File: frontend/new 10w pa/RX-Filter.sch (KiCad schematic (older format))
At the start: 96 parts, among them Q4 FDV301, U3 74LS145

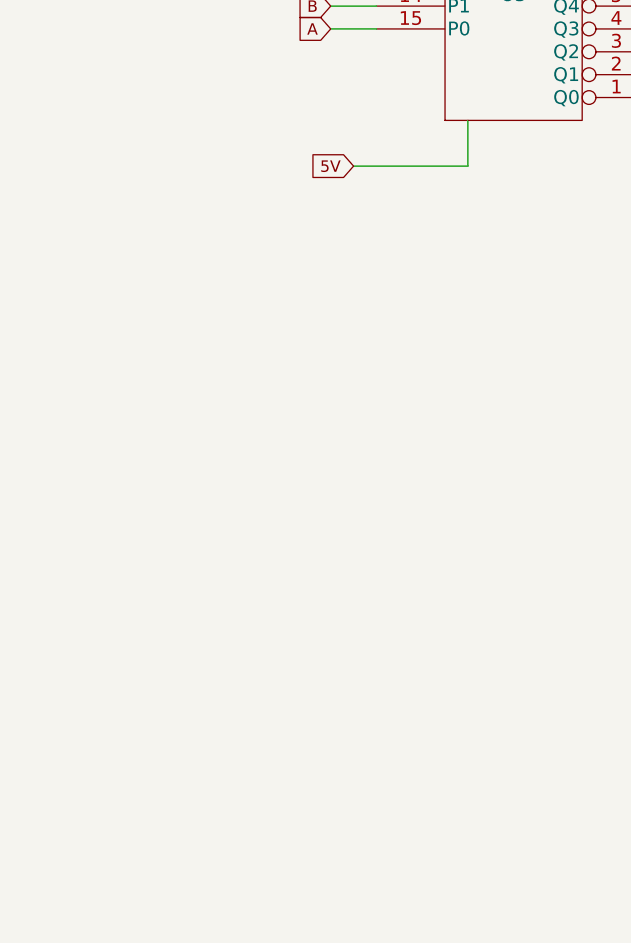
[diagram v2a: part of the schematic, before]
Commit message: Added opto and change of PTT
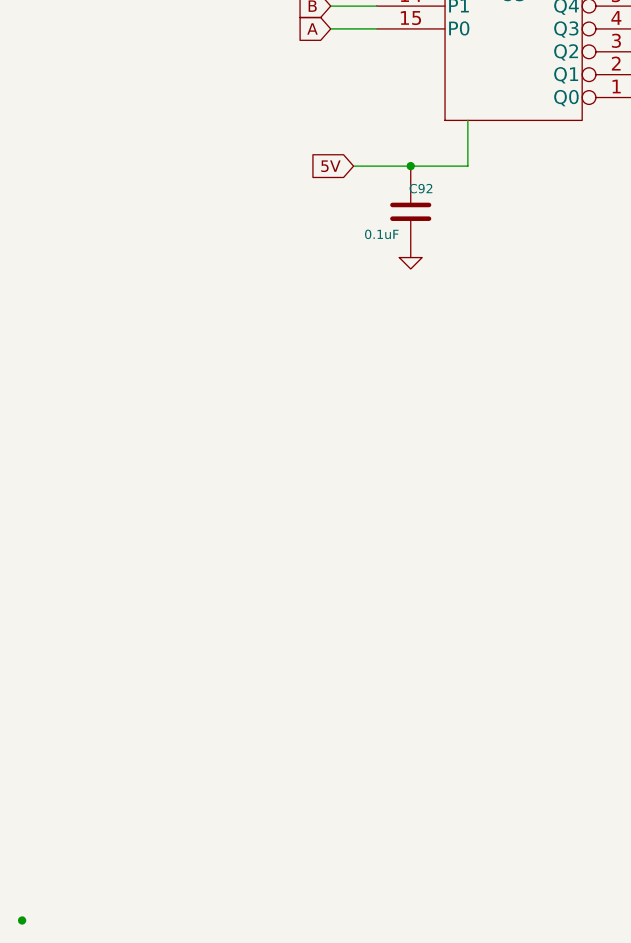
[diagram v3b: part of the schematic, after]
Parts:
- added C92: 0.1uF, HERMESLITE:C_0805, symbol C
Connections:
- net GND: now also C92.1
- net VCC: now also C92.2
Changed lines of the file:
@@
 $EndComp
 $Comp
-L GND #PWR045
+L GND #PWR052
 U 1 1 54A26D4B
 P 7800 2700
-F 0 "#PWR045" H 7800 2700 30  0001 C CNN
+F 0 "#PWR052" H 7800 2700 30  0001 C CNN
 F 1 "GND" H 7800 2630 30  0001 C CNN
 F 2 "" H 7800 2700 50  0000 C CNN
@@
 $EndComp
 $Comp
-L GND #PWR046
+L GND #PWR053
 U 1 1 54A26D51
 P 6550 2700
-F 0 "#PWR046" H 6550 2700 30  0001 C CNN
+F 0 "#PWR053" H 6550 2700 30  0001 C CNN
 F 1 "GND" H 6550 2630 30  0001 C CNN
 F 2 "" H 6550 2700 50  0000 C CNN
@@
 $EndComp
 $Comp
-L GND #PWR047
+L GND #PWR054
 U 1 1 54A26D57
 P 6300 2900
-F 0 "#PWR047" H 6300 2900 30  0001 C CNN
+F 0 "#PWR054" H 6300 2900 30  0001 C CNN
 F 1 "GND" H 6300 2830 30  0001 C CNN
 F 2 "" H 6300 2900 50  0000 C CNN
@@
 $EndComp
 $Comp
-L GND #PWR048
+L GND #PWR055
 U 1 1 54A26D5D
 P 5300 2700
-F 0 "#PWR048" H 5300 2700 30  0001 C CNN
+F 0 "#PWR055" H 5300 2700 30  0001 C CNN
 F 1 "GND" H 5300 2630 30  0001 C CNN
 F 2 "" H 5300 2700 50  0000 C CNN
@@
 $EndComp
 $Comp
-L GND #PWR049
+L GND #PWR056
 U 1 1 54A26D72
 P 4650 3000
-F 0 "#PWR049" H 4650 3000 30  0001 C CNN
+F 0 "#PWR056" H 4650 3000 30  0001 C CNN
 F 1 "GND" H 4650 2930 30  0001 C CNN
 F 2 "" H 4650 3000 50  0000 C CNN
@@
 $EndComp
 $Comp
-L GND #PWR050
+L GND #PWR057
 U 1 1 54A26D78
 P 7950 3000
-F 0 "#PWR050" H 7950 3000 30  0001 C CNN
+F 0 "#PWR057" H 7950 3000 30  0001 C CNN
 F 1 "GND" H 7950 2930 30  0001 C CNN
 F 2 "" H 7950 3000 50  0000 C CNN
@@
 $EndComp
 $Comp
-L GND #PWR051
+L GND #PWR058
 U 1 1 54A28AFC
 P 7800 4700
-F 0 "#PWR051" H 7800 4700 30  0001 C CNN
+F 0 "#PWR058" H 7800 4700 30  0001 C CNN
 F 1 "GND" H 7800 4630 30  0001 C CNN
 F 2 "" H 7800 4700 50  0000 C CNN
@@
 $EndComp
 $Comp
-L GND #PWR052
+L GND #PWR059
 U 1 1 54A28B02
 P 6550 4700
-F 0 "#PWR052" H 6550 4700 30  0001 C CNN
+F 0 "#PWR059" H 6550 4700 30  0001 C CNN
 F 1 "GND" H 6550 4630 30  0001 C CNN
 F 2 "" H 6550 4700 50  0000 C CNN
@@
 $EndComp
 $Comp
-L GND #PWR053
+L GND #PWR060
 U 1 1 54A28B08
 P 6300 4900
-F 0 "#PWR053" H 6300 4900 30  0001 C CNN
+F 0 "#PWR060" H 6300 4900 30  0001 C CNN
 F 1 "GND" H 6300 4830 30  0001 C CNN
 F 2 "" H 6300 4900 50  0000 C CNN
@@
 $EndComp
 $Comp
-L GND #PWR054
+L GND #PWR061
 U 1 1 54A28B0E
 P 5300 4700
-F 0 "#PWR054" H 5300 4700 30  0001 C CNN
+F 0 "#PWR061" H 5300 4700 30  0001 C CNN
 F 1 "GND" H 5300 4630 30  0001 C CNN
 F 2 "" H 5300 4700 50  0000 C CNN
@@
 $EndComp
 $Comp
-L GND #PWR055
+L GND #PWR062
 U 1 1 54A28B21
 P 4650 5000
-F 0 "#PWR055" H 4650 5000 30  0001 C CNN
+F 0 "#PWR062" H 4650 5000 30  0001 C CNN
 F 1 "GND" H 4650 4930 30  0001 C CNN
 F 2 "" H 4650 5000 50  0000 C CNN
@@
 $EndComp
 $Comp
-L GND #PWR056
+L GND #PWR063
 U 1 1 54A28B27
 P 7950 5000
-F 0 "#PWR056" H 7950 5000 30  0001 C CNN
+F 0 "#PWR063" H 7950 5000 30  0001 C CNN
 F 1 "GND" H 7950 4930 30  0001 C CNN
 F 2 "" H 7950 5000 50  0000 C CNN
@@
 $EndComp
 $Comp
-L GND #PWR057
+L GND #PWR064
 U 1 1 54A2A84A
 P 7800 3700
-F 0 "#PWR057" H 7800 3700 30  0001 C CNN
+F 0 "#PWR064" H 7800 3700 30  0001 C CNN
 F 1 "GND" H 7800 3630 30  0001 C CNN
 F 2 "" H 7800 3700 50  0000 C CNN
@@
 $EndComp
 $Comp
-L GND #PWR058
+L GND #PWR065
 U 1 1 54A2A850
 P 6550 3700
-F 0 "#PWR058" H 6550 3700 30  0001 C CNN
+F 0 "#PWR065" H 6550 3700 30  0001 C CNN
 F 1 "GND" H 6550 3630 30  0001 C CNN
 F 2 "" H 6550 3700 50  0000 C CNN
@@
 $EndComp
 $Comp
-L GND #PWR059
+L GND #PWR066
 U 1 1 54A2A856
 P 6300 3900
-F 0 "#PWR059" H 6300 3900 30  0001 C CNN
+F 0 "#PWR066" H 6300 3900 30  0001 C CNN
 F 1 "GND" H 6300 3830 30  0001 C CNN
 F 2 "" H 6300 3900 50  0000 C CNN
@@
 $EndComp
 $Comp
-L GND #PWR060
+L GND #PWR067
 U 1 1 54A2A85C
 P 5300 3700
-F 0 "#PWR060" H 5300 3700 30  0001 C CNN
+F 0 "#PWR067" H 5300 3700 30  0001 C CNN
 F 1 "GND" H 5300 3630 30  0001 C CNN
 F 2 "" H 5300 3700 50  0000 C CNN
@@
 $EndComp
 $Comp
-L GND #PWR061
+L GND #PWR068
 U 1 1 54A2A86F
 P 4650 4000
-F 0 "#PWR061" H 4650 4000 30  0001 C CNN
+F 0 "#PWR068" H 4650 4000 30  0001 C CNN
 F 1 "GND" H 4650 3930 30  0001 C CNN
 F 2 "" H 4650 4000 50  0000 C CNN
@@
 $EndComp
 $Comp
-L GND #PWR062
+L GND #PWR069
 U 1 1 54A2A875
 P 7950 4000
-F 0 "#PWR062" H 7950 4000 30  0001 C CNN
+F 0 "#PWR069" H 7950 4000 30  0001 C CNN
 F 1 "GND" H 7950 3930 30  0001 C CNN
 F 2 "" H 7950 4000 50  0000 C CNN
@@
 $EndComp
 $Comp
-L GND #PWR063
+L GND #PWR070
 U 1 1 54A2AFAC
 P 7800 5700
-F 0 "#PWR063" H 7800 5700 30  0001 C CNN
+F 0 "#PWR070" H 7800 5700 30  0001 C CNN
 F 1 "GND" H 7800 5630 30  0001 C CNN
 F 2 "" H 7800 5700 50  0000 C CNN
@@
 $EndComp
 $Comp
-L GND #PWR064
+L GND #PWR071
 U 1 1 54A2AFB2
 P 6550 5700
-F 0 "#PWR064" H 6550 5700 30  0001 C CNN
+F 0 "#PWR071" H 6550 5700 30  0001 C CNN
 F 1 "GND" H 6550 5630 30  0001 C CNN
 F 2 "" H 6550 5700 50  0000 C CNN
@@
 $EndComp
 $Comp
-L GND #PWR065
+L GND #PWR072
 U 1 1 54A2AFB8
 P 6300 5900
-F 0 "#PWR065" H 6300 5900 30  0001 C CNN
+F 0 "#PWR072" H 6300 5900 30  0001 C CNN
 F 1 "GND" H 6300 5830 30  0001 C CNN
 F 2 "" H 6300 5900 50  0000 C CNN
@@
 $EndComp
 $Comp
-L GND #PWR066
+L GND #PWR073
 U 1 1 54A2AFBE
 P 5200 5700
-F 0 "#PWR066" H 5200 5700 30  0001 C CNN
+F 0 "#PWR073" H 5200 5700 30  0001 C CNN
 F 1 "GND" H 5200 5630 30  0001 C CNN
 F 2 "" H 5200 5700 50  0000 C CNN
@@
 $EndComp
 $Comp
-L GND #PWR067
+L GND #PWR074
 U 1 1 54A2AFD1
 P 4600 6000
-F 0 "#PWR067" H 4600 6000 30  0001 C CNN
+F 0 "#PWR074" H 4600 6000 30  0001 C CNN
 F 1 "GND" H 4600 5930 30  0001 C CNN
 F 2 "" H 4600 6000 50  0000 C CNN
@@
 $EndComp
 $Comp
-L GND #PWR068
+L GND #PWR075
 U 1 1 54A2AFD7
 P 8050 6000
-F 0 "#PWR068" H 8050 6000 30  0001 C CNN
+F 0 "#PWR075" H 8050 6000 30  0001 C CNN
 F 1 "GND" H 8050 5930 30  0001 C CNN
 F 2 "" H 8050 6000 50  0000 C CNN
@@
 $EndComp
 $Comp
-L GND #PWR069
+L GND #PWR076
 U 1 1 54A2CBBC
 P 6550 6700
-F 0 "#PWR069" H 6550 6700 30  0001 C CNN
+F 0 "#PWR076" H 6550 6700 30  0001 C CNN
 F 1 "GND" H 6550 6630 30  0001 C CNN
 F 2 "" H 6550 6700 50  0000 C CNN
@@
 $EndComp
 $Comp
-L GND #PWR070
+L GND #PWR077
 U 1 1 54A2CBCE
 P 5300 6700
-F 0 "#PWR070" H 5300 6700 30  0001 C CNN
+F 0 "#PWR077" H 5300 6700 30  0001 C CNN
 F 1 "GND" H 5300 6630 30  0001 C CNN
 F 2 "" H 5300 6700 50  0000 C CNN
@@
 $EndComp
 $Comp
-L GND #PWR071
+L GND #PWR078
 U 1 1 54A2CBE1
 P 4650 7000
-F 0 "#PWR071" H 4650 7000 30  0001 C CNN
+F 0 "#PWR078" H 4650 7000 30  0001 C CNN
 F 1 "GND" H 4650 6930 30  0001 C CNN
 F 2 "" H 4650 7000 50  0000 C CNN
@@
 $EndComp
 $Comp
-L GND #PWR072
+L GND #PWR079
 U 1 1 54A2CBE7
 P 6800 7000
-F 0 "#PWR072" H 6800 7000 30  0001 C CNN
+F 0 "#PWR079" H 6800 7000 30  0001 C CNN
 F 1 "GND" H 6800 6930 30  0001 C CNN
 F 2 "" H 6800 7000 50  0000 C CNN
@@
 Filter Settings for PowerSDR Hermes Ctrl\n(set for RX and TX J16 Pins)\n        1  2  3  4 \nBypass 0  1  0  1 (or higher) \n160M   0  0  0  0\n80M    1  0  0  0\n60M    0  1  0  0\n40M    1  1  0  0\n30M    0  0  1  0\n20M    1  0  1  0\n17M    0  1  1  0\n15M    1  1  1  0\n12M    0  0  0  1\n10M    1  0  0  1
 $Comp
-L GND #PWR073
+L GND #PWR080
 U 1 1 54C1EBE4
 P 1150 3100
-F 0 "#PWR073" H 1150 3100 30  0001 C CNN
+F 0 "#PWR080" H 1150 3100 30  0001 C CNN
 F 1 "GND" H 1150 3030 30  0001 C CNN
 F 2 "" H 1150 3100 50  0000 C CNN
@@
 $EndComp
 $Comp
-L GND #PWR074
+L GND #PWR081
 U 1 1 54C3258A
 P 4900 2000
-F 0 "#PWR074" H 4900 2000 30  0001 C CNN
+F 0 "#PWR081" H 4900 2000 30  0001 C CNN
 F 1 "GND" H 4900 1930 30  0001 C CNN
 F 2 "" H 4900 2000 50  0000 C CNN
@@
 $EndComp
 $Comp
-L GND #PWR075
+L GND #PWR082
 U 1 1 54C32686
 P 7900 2000
-F 0 "#PWR075" H 7900 2000 30  0001 C CNN
+F 0 "#PWR082" H 7900 2000 30  0001 C CNN
 F 1 "GND" H 7900 1930 30  0001 C CNN
 F 2 "" H 7900 2000 50  0000 C CNN
@@
 	3200 1900 3100 1900
 $Comp
-L GND #PWR076
+L GND #PWR083
 U 1 1 54C40367
 P 3100 2400
-F 0 "#PWR076" H 3100 2400 30  0001 C CNN
+F 0 "#PWR083" H 3100 2400 30  0001 C CNN
 F 1 "GND" H 3100 2330 30  0001 C CNN
 F 2 "" H 3100 2400 50  0000 C CNN
@@
 	6300 6300 6300 6500
 Connection ~ 6350 6300
+$Comp
+L C C92
+U 1 1 54D8F694
+P 1150 4600
+F 0 "C92" H 1050 4500 40  0000 L CNN
+F 1 "0.1uF" H 1200 4700 40  0000 L CNN
+F 2 "HERMESLITE:C_0805" H 1188 4450 30  0001 C CNN
+F 3 "" H 1150 4600 60  0000 C CNN
+	1    1150 4600
+	-1   0    0    1
+$EndComp
+$Comp
+L GND #PWR084
+U 1 1 54D8FD7B
+P 1150 4800
+F 0 "#PWR084" H 1150 4800 30  0001 C CNN
+F 1 "GND" H 1150 4730 30  0001 C CNN
+F 2 "" H 1150 4800 50  0000 C CNN
+F 3 "" H 1150 4800 50  0000 C CNN
+	1    1150 4800
+	1    0    0    -1
+$EndComp
+Connection ~ 1150 4400
+Connection ~ -550 7700
 $EndSCHEMATC

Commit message: modify mounting holes
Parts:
- Q4: footprint SMD_Packages:SOT-23-GDS -> HERMESLITE:SOT-23-GDS
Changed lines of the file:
@@
 F 0 "Q4" H 3010 2270 60  0000 R CNN
 F 1 "FDV301" H 2850 2250 60  0000 R CNN
-F 2 "SMD_Packages:SOT-23-GDS" H 3000 2100 60  0001 C CNN
+F 2 "HERMESLITE:SOT-23-GDS" H 3000 2100 60  0001 C CNN
 F 3 "" H 3000 2100 60  0000 C CNN
 	1    3000 2100
